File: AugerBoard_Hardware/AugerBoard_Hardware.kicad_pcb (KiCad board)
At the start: 2 copper layers, 88.9 x 82.5 mm, 51 parts, among them J1 RJ45_LED_Shielded, J2 Conn_01x04_MountingPin, Q1 BSS138, Q2 BSS138, Q3 BSS138, SW1 SW_SPDT, SW2 SW_Push, SW3 SW_Push, SW4 SW_Push, U1 Teensy4.1_DEV-16771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

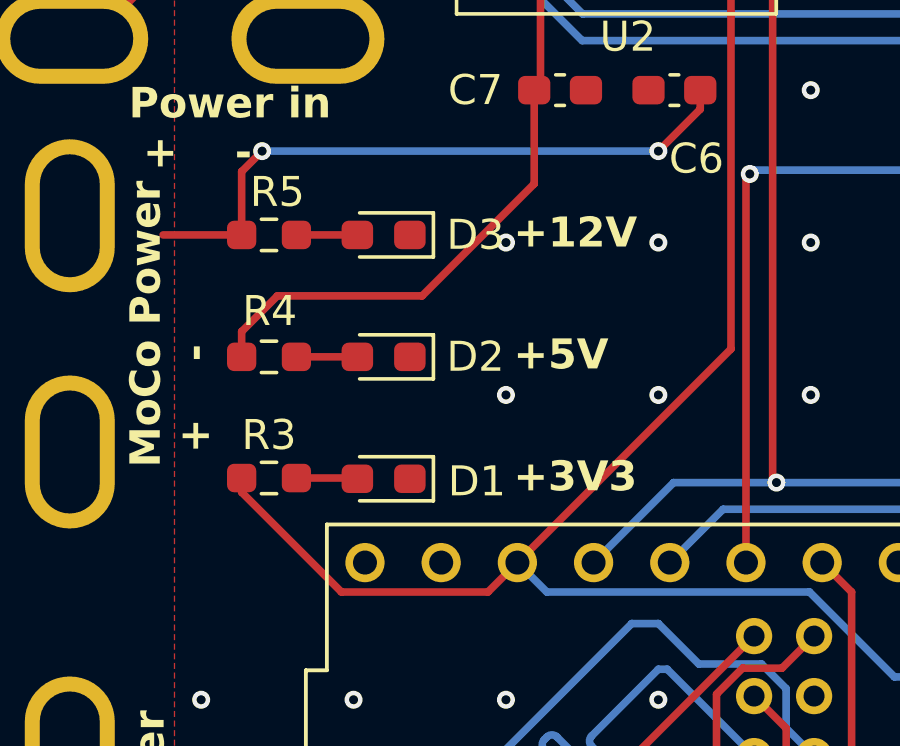
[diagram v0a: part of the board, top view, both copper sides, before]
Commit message: 5 volt to teensy fixed (single worst trace ever made)
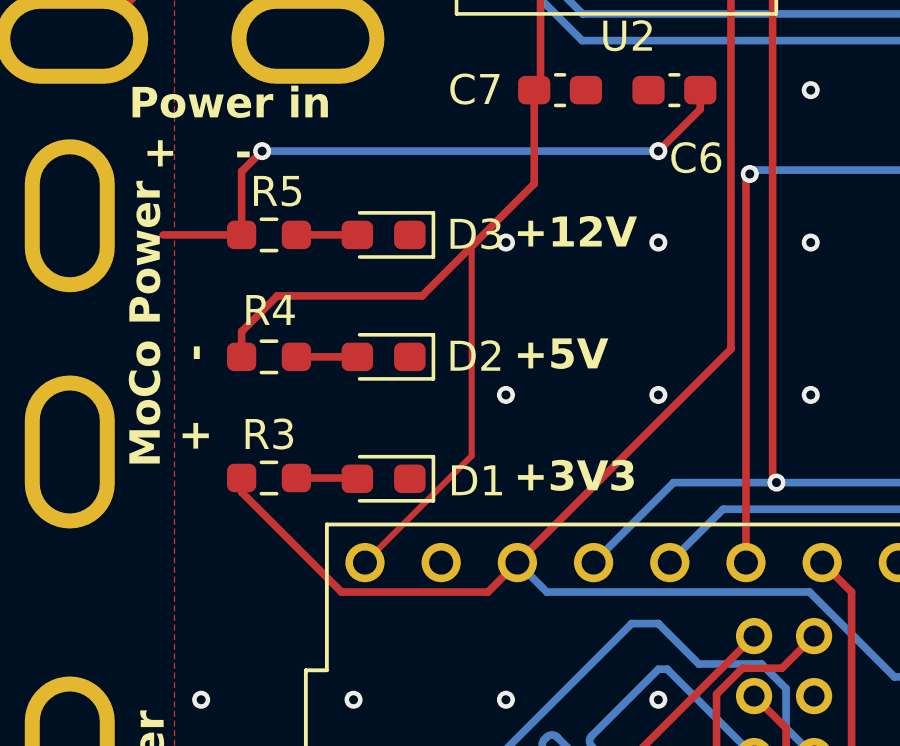
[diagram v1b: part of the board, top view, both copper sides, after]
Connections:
- U1 pad VIN: unconnected-(U1-PadVIN) -> +5V
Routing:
- net +5V: track 207.7 -> 219.7 mm

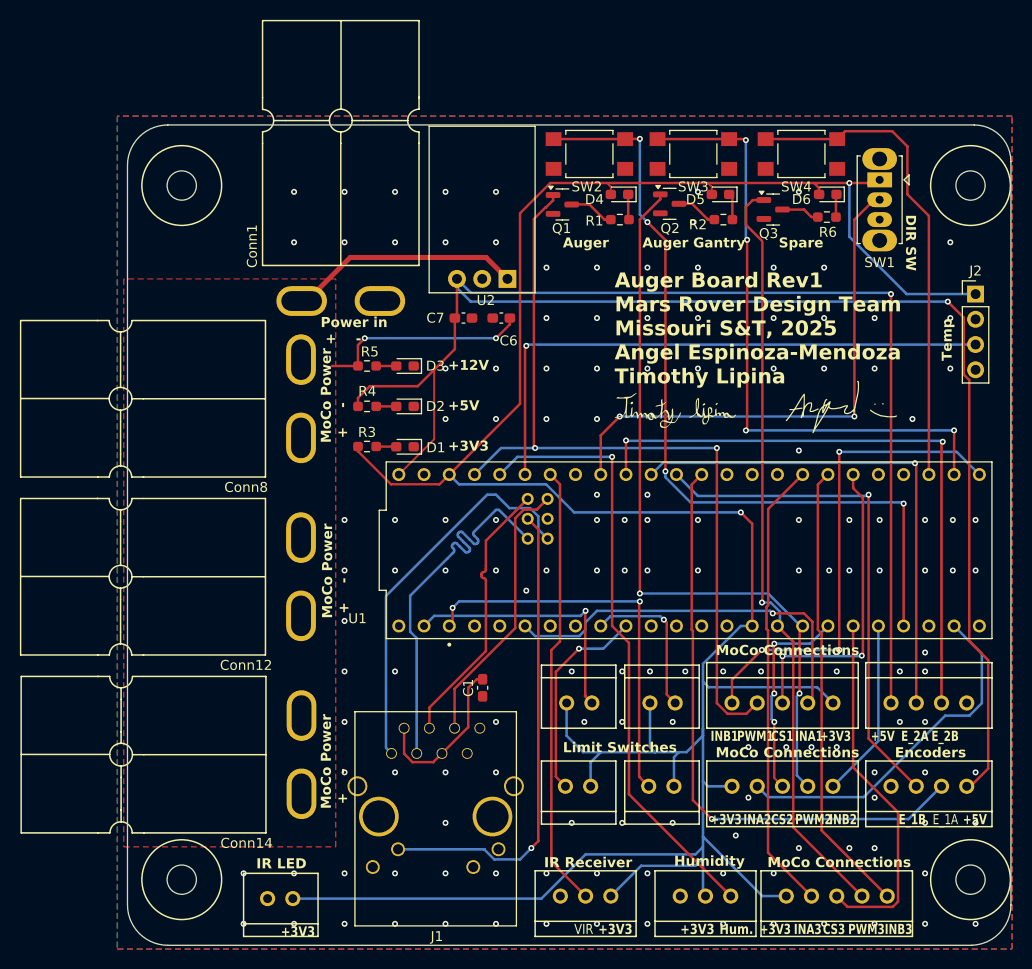
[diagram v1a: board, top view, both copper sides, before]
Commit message: UV Led connection added
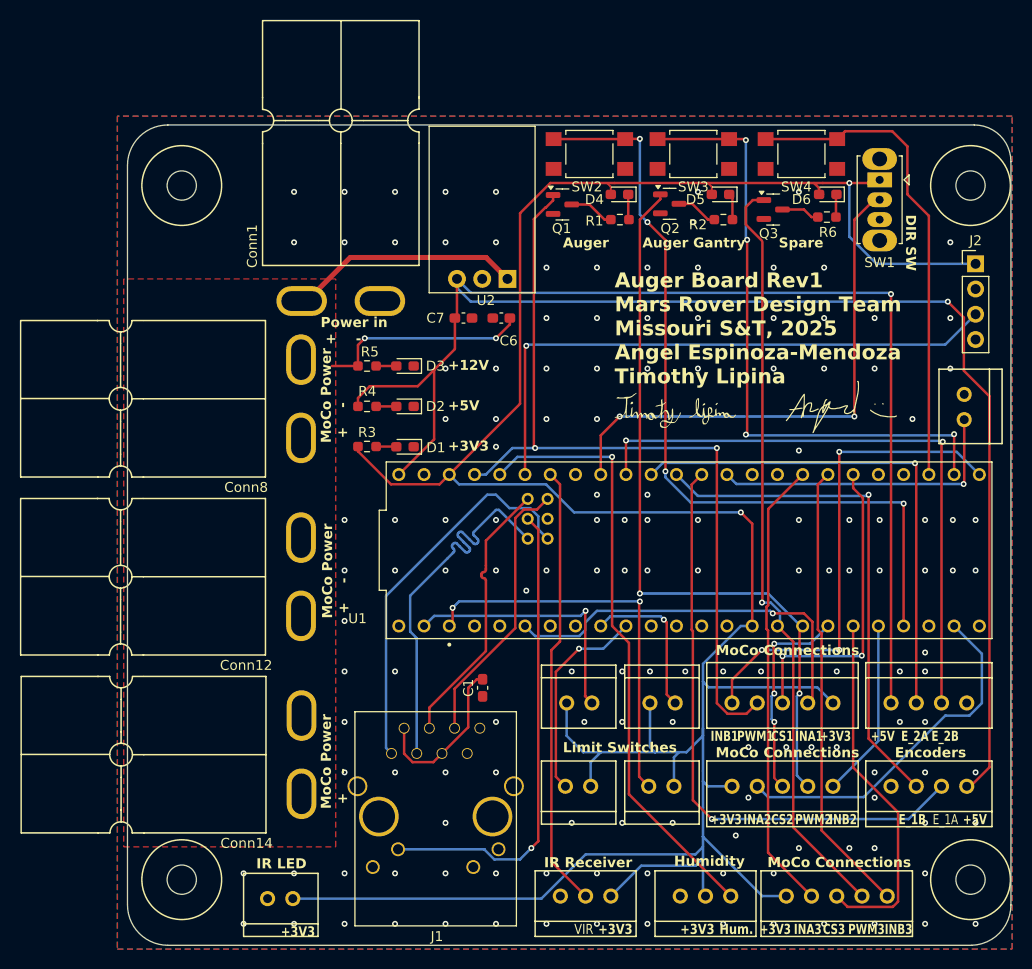
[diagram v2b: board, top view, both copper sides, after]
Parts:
- added Conn17: Molex_SL_02, MRDT_Connectors:MOLEX_SL_02_Vertical, F.Cu at (158.9, 99.1)
- moved J2 3.05 mm to (160.0, 86.0)
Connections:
- U1 pad 13: unconnected-(U1-SCK-Pad13) -> UV Led
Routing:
- net UV Led: track 0.00 -> 30.8 mm, vias 0 -> 1
- net Temp: track 58.3 -> 59.5 mm
- net +3.3V: track 291.5 -> 290.3 mm
- net GND: vias 147 -> 148
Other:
- board text removed: "Temp"

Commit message: vesc connections added, some traces rerouted, silkscreens added
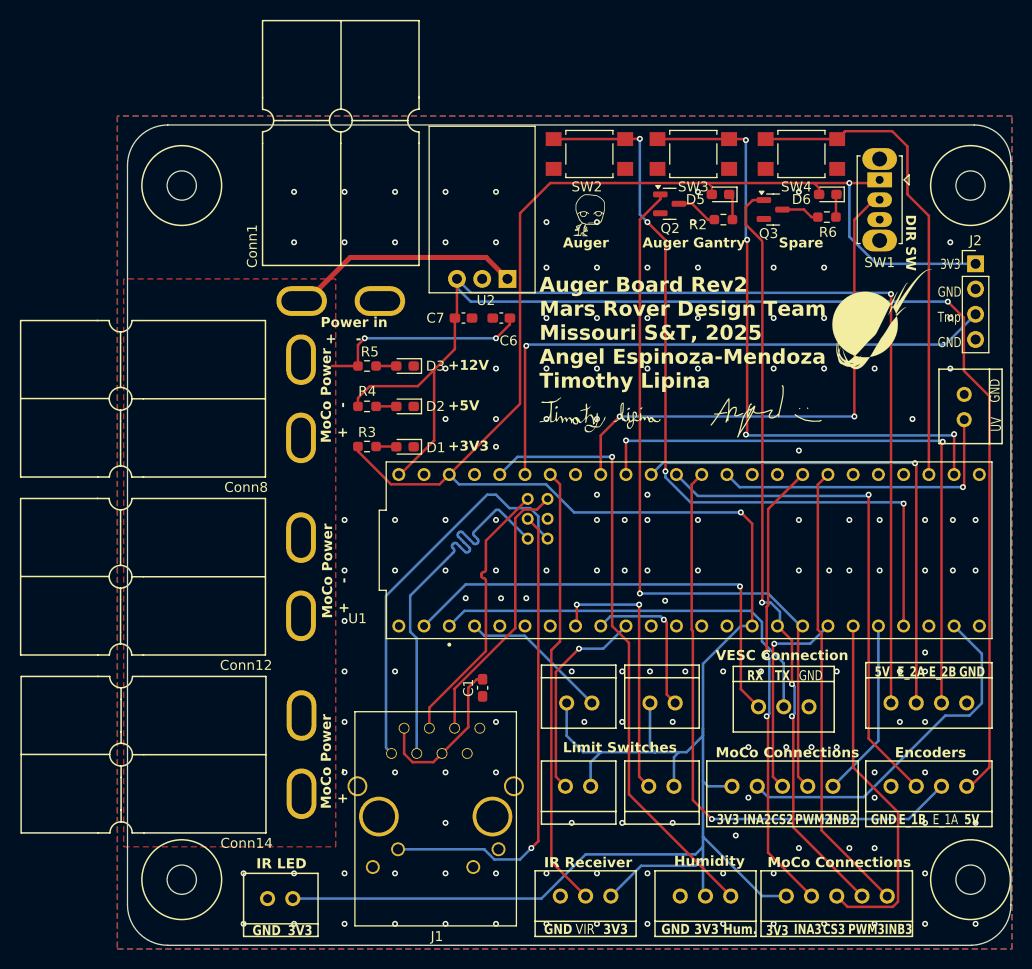
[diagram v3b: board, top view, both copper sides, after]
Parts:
- removed Conn9: Molex_SL_05, MRDT_Connectors:MOLEX_SL_05_Vertical
- removed D4: Blue, LED_SMD:LED_0603_1608Metric_Pad1.05x0.95mm_HandSolder
- removed Q1: BSS138, Package_TO_SOT_SMD:SOT-23
- removed R1: 220, Resistor_SMD:R_0603_1608Metric_Pad0.98x0.95mm_HandSolder
- removed ‎ : LOGO, LOGO
- added Conn18: Molex_SL_03, MRDT_Connectors:MOLEX_SL_03_Vertical, F.Cu at (138.2, 130.6)
- added G***: LOGO, MRDT_Silkscreens:0_MRDT_Logo_10mm, F.Cu at (150.6, 91.6)
- added ‎: LOGO, LOGO, F.Cu at (120.9, 81.3)
- added ‎: LOGO, LOGO, B.Cu at (125.9, 88.6)
- added ‎‎: LOGO, LOGO, B.Cu at (94.1, 138.0)
- moved G*** 7.59 mm to (125.2, 101.2)
- moved ‎ 7.59 mm to (139.0, 101.2)
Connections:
- U1 pad 0: LimitSwitch1 -> Aug_RX
- U1 pad 1: LimitSwitch2 -> Aug_TX
- U1 pad 2: unconnected-(U1-OUT2-Pad2) -> LimitSwitch1
- U1 pad 23: PWM1 -> unconnected-(U1-A9-Pad23)
- U1 pad 33: IN_B1 -> unconnected-(U1-MCLK2-Pad33)
- U1 pad 38: CS1 -> unconnected-(U1-A14-Pad38)
- U1 pad 4: IN_A1 -> unconnected-(U1-BCLK2-Pad4)
- U1 pad 6: unconnected-(U1-OUT1D-Pad6) -> LimitSwitch2
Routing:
- net PWM1: track 82.5 -> 0.00 mm, vias 2 -> 0
- net IN_B1: track 49.4 -> 0.00 mm, vias 3 -> 0
- net Aug_RX: track 0.00 -> 46.5 mm, vias 0 -> 1
- net Aug_TX: track 0.00 -> 42.5 mm
- net IN_A1: track 39.7 -> 0.00 mm, vias 1 -> 0
- net CS1: track 31.4 -> 0.00 mm, vias 2 -> 0
- net +3.3V: track 290.3 -> 274.2 mm
- net LimitSwitch2: track 40.1 -> 27.2 mm
- net LimitSwitch1: track 26.5 -> 15.2 mm, vias 1 -> 0
- net Net-(Q1-D): track 4.57 -> 0.00 mm
- net Net-(D4-K): track 2.57 -> 0.00 mm
- net CS2: track 21.1 -> 22.1 mm, vias 3 -> 1
- net IN_A3: track 45.8 -> 46.0 mm, vias 0 -> 2
- net PWM3: track 76.9 -> 77.2 mm, vias 1 -> 3
- net PWM2: track 75.6 -> 75.5 mm, vias 2 -> 1
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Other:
- board text added: "3V3"
- board text added: "5V"
- board text added: "Auger Board Rev2 Mars Rover Design Team Missouri S&T, 2025 Angel Espinoza-Mendoza Timothy Lipina"
- board text added: "GND"
- board text added: "RX"
- board text added: "TX"
- board text added: "Tmp"
- board text added: "UV"
- board text added: "VESC Connection"
- board text removed: "Auger Board Rev1 Mars Rover Design Team Missouri S&T, 2025 Angel Espinoza-Mendoza Timothy Lipina"
- board text removed: "CS1"
- board text removed: "INA1"
- board text removed: "INB1"
- board text removed: "PWM1"

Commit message: just one more drawing i swear
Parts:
- added ‎: LOGO, LOGO, B.Cu at (93.5, 107.4)

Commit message: slight adjustment
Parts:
- moved ‎ 1.61 mm to (93.7, 105.9)

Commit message: Schematic probably correct, layout fucked
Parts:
- removed Conn2: Molex_SL_04, MRDT_Connectors:MOLEX_SL_04_Vertical
- removed Conn5: Molex_SL_02, MRDT_Connectors:MOLEX_SL_02_Vertical
- added Conn7: Molex_SL_03, MRDT_Connectors:MOLEX_SL_03_Vertical, F.Cu at (158.9, 132.2)
- added Conn7: Molex_SL_03, MRDT_Connectors:MOLEX_SL_03_Vertical, F.Cu at (152.4, 129.3)
- moved Conn3 12.1 mm to (144.5, 140.1)
- moved Conn13 8.00 mm to (137.7, 138.4)
- moved Conn18 2.30 mm to (135.9, 130.8)
- moved Conn11 0.63 mm to (120.7, 138.6)
- moved Conn7 0.63 mm to (134.7, 149.6)
- moved Conn15 0.25 mm to (151.4, 149.6)
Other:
- board text removed: "5V"
- board text removed: "CS2"
- board text removed: "E_1A"
- board text removed: "E_1B"
- board text removed: "E_2A"
- board text removed: "E_2B"
- board text removed: "INA2"
- board text removed: "INB2"
- board text removed: "PWM2"

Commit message: Layout and retracing
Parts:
- removed Conn11: Molex_SL_02, MRDT_Connectors:MOLEX_SL_02_Vertical
- removed Conn3: Molex_SL_04, MRDT_Connectors:MOLEX_SL_04_Vertical
- removed the Conn7 at (158.9, 132.2)
- removed the Conn7 at (152.4, 129.3)
- added Conn19: Molex_SL_03, MRDT_Connectors:MOLEX_SL_03_Vertical, F.Cu at (158.8, 131.3)
- added Conn2: Molex_SL_04, MRDT_Connectors:MOLEX_SL_04_Vertical, F.Cu at (143.5, 141.6)
- added Conn5: Molex_SL_02, MRDT_Connectors:MOLEX_SL_02_Vertical, F.Cu at (126.6, 130.2)
- added Conn9: Molex_SL_03, MRDT_Connectors:MOLEX_SL_03_Vertical, F.Cu at (146.1, 130.4)
- moved Conn10 14.4 mm to (118.2, 141.4)
- moved Conn13 11.1 mm to (127.0, 141.6), turned to 0 degrees
- moved Conn18 0.97 mm to (135.0, 130.4)
- moved Conn4 0.64 mm to (118.2, 130.2)
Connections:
- U1 pad 0: Aug_RX -> unconnected-(U1-RX1-Pad0)
- U1 pad 1: Aug_TX -> unconnected-(U1-TX1-Pad1)
- U1 pad 10: unconnected-(U1-CS1-Pad10) -> LimitSwitch2
- U1 pad 12: unconnected-(U1-MISO-Pad12) -> IN_A2
- U1 pad 13: UV Led -> SW2
- U1 pad 14: Encoder_1a -> CS2
- U1 pad 15: Encoder_1b -> PWM2
- U1 pad 16: Encoder_2a -> SW1
- U1 pad 17: Encoder_2b -> Humidity
- U1 pad 18: Dir_Switch -> unconnected-(U1-A4-Pad18)
- U1 pad 2: LimitSwitch1 -> unconnected-(U1-OUT2-Pad2)
- U1 pad 21: Temp -> unconnected-(U1-A7-Pad21)
- U1 pad 22: Humidity -> unconnected-(U1-A8-Pad22)
- U1 pad 25: PWM2 -> unconnected-(U1-A11-Pad25)
- U1 pad 26: CS2 -> Encoder_1a
- U1 pad 28: IN_B2 -> Encoder_1b
- U1 pad 29: SW1 -> ServoPWM1
- U1 pad 31: IN_A2 -> unconnected-(U1-CTX3-Pad31)
- U1 pad 32: unconnected-(U1-OUT1B-Pad32) -> IN_B3
- U1 pad 33: unconnected-(U1-MCLK2-Pad33) -> ServoPWM2
- U1 pad 34: SW2 -> UV Led
- U1 pad 37: unconnected-(U1-CS3-Pad37) -> Dir_Switch
- U1 pad 38: unconnected-(U1-A14-Pad38) -> Temp
- U1 pad 39: IN_B3 -> unconnected-(U1-A15-Pad39)
- U1 pad 4: unconnected-(U1-BCLK2-Pad4) -> LimitSwitch3
- U1 pad 40: IN_A3 -> unconnected-(U1-A16-Pad40)
- U1 pad 41: unconnected-(U1-A17-Pad41) -> IN_A3
- U1 pad 6: LimitSwitch2 -> LimitSwitch1
- U1 pad 7: LimitSwitch3 -> Aug_RX
- U1 pad 8: LimitSwitch4 -> Aug_TX
- U1 pad 9: unconnected-(U1-OUT1C-Pad9) -> IN_B2
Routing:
- net Encoder_2b: track 61.7 -> 0.00 mm, vias 2 -> 0
- net Encoder_2a: track 51.2 -> 0.00 mm, vias 1 -> 0
- net Encoder_1a: track 60.4 -> 19.8 mm, vias 1 -> 0
- net SW1: track 81.2 -> 42.7 mm, vias 4 -> 2
- net Temp: track 59.5 -> 21.2 mm, vias 1 -> 0
- net Encoder_1b: track 51.6 -> 20.3 mm, vias 1 -> 0
- net Aug_RX: track 46.5 -> 16.0 mm, vias 1 -> 0
- net ServoPWM2: track 0.00 -> 28.6 mm
- net Aug_TX: track 42.5 -> 16.0 mm
- net +3.3V: track 274.2 -> 300.6 mm
- net UV Led: track 31.2 -> 5.95 mm, vias 1 -> 0
- net Dir_Switch: track 53.4 -> 30.3 mm, vias 2 -> 0
- net LimitSwitch4: track 20.9 -> 0.00 mm, vias 1 -> 0
- net SW2: track 63.7 -> 43.0 mm, vias 4 -> 2
- net LimitSwitch2: track 27.2 -> 8.06 mm, vias 2 -> 0
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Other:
- board text added: "Encoder"
- board text added: "MoCo"
- board text added: "Servo"
- board text added: "UV LED"
- board text added: "VESC"
- board text removed: "Encoders"
- board text removed: "MoCo Connections"
- board text removed: "VESC Connection"

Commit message: Small schematic and layout fixes
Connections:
- Conn13 pad 1: IN_B2 -> IN_B1
- Conn13 pad 2: PWM2 -> PWM1
- Conn13 pad 3: CS2 -> CS1
- Conn13 pad 4: IN_A2 -> IN_A1
- Conn15 pad 1: IN_B3 -> IN_B2
- Conn15 pad 2: PWM3 -> PWM2
- Conn15 pad 3: CS3 -> CS2
- Conn15 pad 4: IN_A3 -> IN_A2
- Q2 pad 1: PWM2 -> PWM1
- Q3 pad 1: PWM3 -> PWM2
- U1 pad 12: IN_A2 -> IN_A1
- U1 pad 14: CS2 -> CS1
- U1 pad 15: PWM2 -> PWM1
- U1 pad 24: PWM3 -> PWM2
- U1 pad 25: unconnected-(U1-A11-Pad25) -> Encoder_1b
- U1 pad 27: CS3 -> CS2
- U1 pad 28: Encoder_1b -> unconnected-(U1-RX7-Pad28)
- U1 pad 30: SW4 -> unconnected-(U1-CRX3-Pad30)
- U1 pad 32: IN_B3 -> IN_B2
- U1 pad 41: IN_A3 -> IN_A2
- U1 pad 9: IN_B2 -> IN_B1
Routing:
- net PWM3: track 76.4 -> 0.00 mm
- net PWM1: track 0.00 -> 66.1 mm
- net IN_A3: track 43.9 -> 0.00 mm
- net CS1: track 0.00 -> 35.1 mm
- net IN_B3: track 30.9 -> 0.00 mm
- net CS3: track 27.8 -> 0.00 mm
- net IN_A2: track 20.3 -> 43.9 mm
- net IN_A1: track 0.00 -> 20.3 mm
- net IN_B1: track 0.00 -> 19.6 mm
- net IN_B2: track 19.6 -> 30.9 mm
- net PWM2: track 66.1 -> 76.4 mm
- net CS2: track 35.1 -> 27.8 mm
- net Encoder_1b: track 20.3 -> 21.9 mm
- net unconnected-(U1-RX7-Pad28): track 0.00 -> 0.83 mm
